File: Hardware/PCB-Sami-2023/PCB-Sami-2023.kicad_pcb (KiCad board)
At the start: 2 copper layers, 75.2 x 32 mm, 16 parts, among them J1 Bateria (+), J10 MOTOR_DER, J2 IR_COSTADO, J3 Sensor TATAMI FD, J5 Sensor TATAMI FI, J6 STEP_DOWN, J7 IR_FD, J8 IR_FI, J9 MOTOR_IZQ, SW1 START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

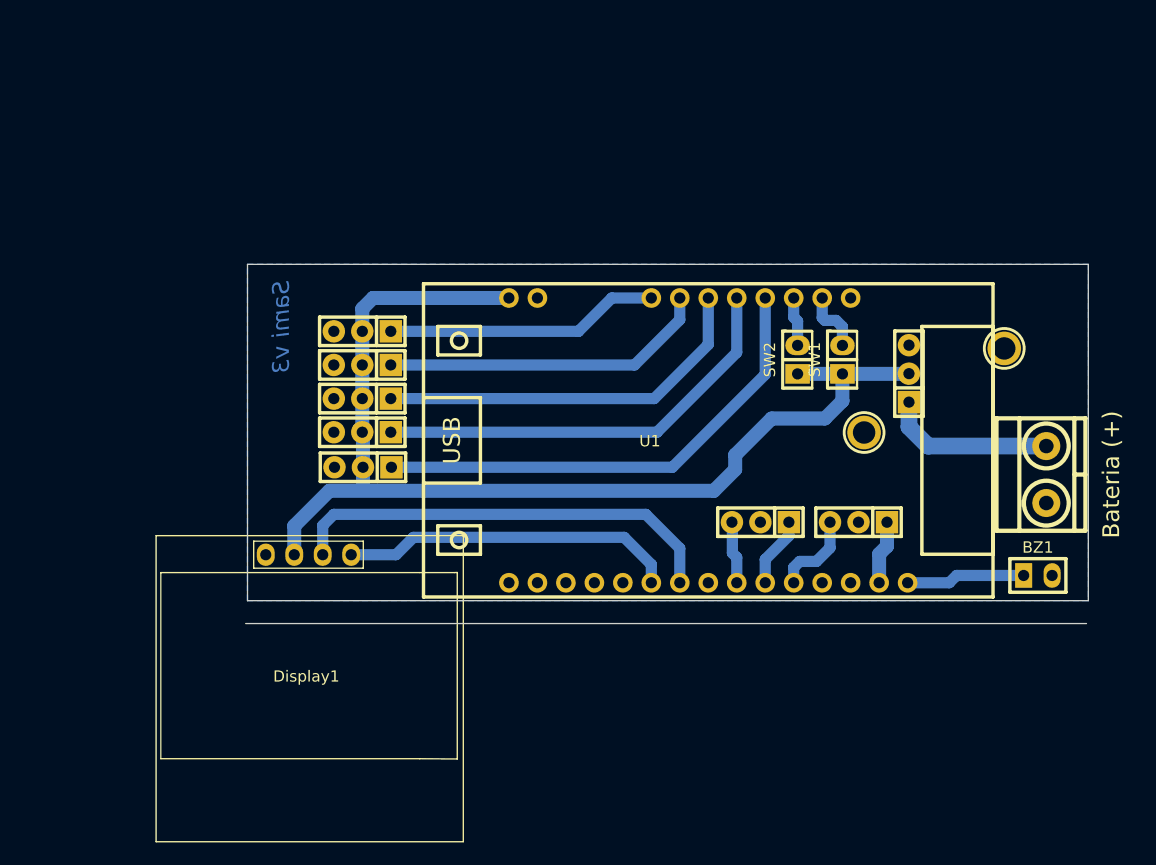
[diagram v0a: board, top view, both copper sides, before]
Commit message: PCB con sus componentes correctamente acomodados, falta solo los agujeros de sujecion y trazar pistas
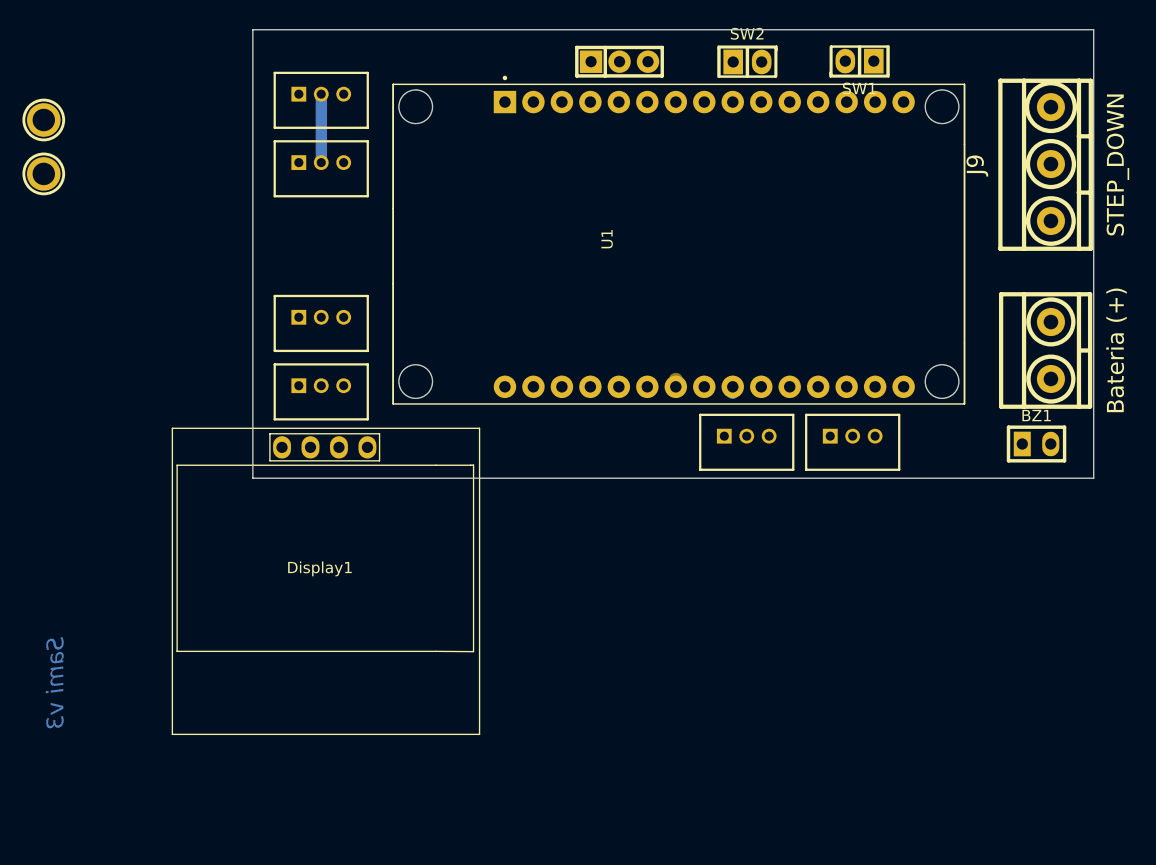
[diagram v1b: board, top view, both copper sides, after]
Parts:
- removed the J10 at (161.2, 95.8)
- removed J2: IR_COSTADO, EESTN5:Pin_Strip_3
- removed J3: Sensor TATAMI FD, EESTN5:Pin_Strip_3
- removed J5: Sensor TATAMI FI, EESTN5:Pin_Strip_3
- removed J6: STEP_DOWN, EESTN5:Pin_Strip_3
- removed J7: IR_FD, EESTN5:Pin_Strip_3
- removed J8: IR_FI, EESTN5:Pin_Strip_3
- added P1: SensorTatamiDerecho, Footprints:JstXH3P, F.Cu at (113.3, 77.5)
- added P2: SensorTatamiIzquierdo, Footprints:JstXH3P, F.Cu at (113.3, 83.6)
- added P3: IFR_DER, Footprints:JstXH3P, F.Cu at (113.3, 57.6)
- added P4: IFR_IZQ, Footprints:JstXH3P, F.Cu at (113.3, 63.7)
- added P5: LDR, EESTN5:Pin_Strip_3, F.Cu at (139.9, 54.7)
- added P6: MotorDerecho, Footprints:JstXH3P, F.Cu at (160.7, 88.1)
- added P7: MotorIzquierdo, Footprints:JstXH3P, F.Cu at (151.2, 88.1)
- J9: value MOTOR_IZQ -> STEP_DOWN; footprint EESTN5:Pin_Strip_3 -> EESTN5:BORNERA3_AZUL
- U1: value ESP32_DevKit_V1_CH9102X -> ESP32-DEVKIT-V1; footprint EESTN5:ESP32_DevKit_V1_CH9102X -> Footprints:ESP32-DEVKIT-V1-30Pines
- moved H1 88.1 mm to (88.5, 59.9)
- moved H2 76.7 mm to (88.5, 64.7)
- moved J9 41.1 mm to (178.4, 63.8), turned to 90 degrees
- moved SW2 27.2 mm to (151.3, 54.4), turned to 0 degrees
- moved SW1 26.4 mm to (161.3, 55.0), turned to 180 degrees
- moved U1 18.4 mm to (145.2, 70.5), turned to 90 degrees
- moved BZ1 11.7 mm to (177.1, 88.8)
- moved J10 11.1 mm to (178.4, 80.5)
- moved Display1 9.68 mm to (113.4, 99.7)
- renumbered J1 to J10
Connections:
- J9 pad 1: /M2B -> GND
- J9 pad 2: GND -> +5V
- J9 pad 3: /M2A -> /Vstep
- U1 pad 10: /TATAMI_FI -> /TATAMI_IZQ
- U1 pad 14: GND -> unconnected-(U1-VP-Pad14)
- U1 pad 15: +5V -> unconnected-(U1-EN-Pad15)
- U1 pad 16: unconnected-(U1-Pad16) -> /BUZZER
- U1 pad 17: GND -> /M1B_DIR
- U1 pad 20: unconnected-(U1-Pad20) -> /M1A_PWM
- U1 pad 21: /SDA -> /M2B_DIR
- U1 pad 22: /SCL -> /M2A_PWM
- U1 pad 24: /M2A -> /SCL
- U1 pad 25: /M2B -> /SDA
- U1 pad 26: /M1A -> unconnected-(U1-D4-Pad26)
- U1 pad 29: /M1B -> GND
- U1 pad 30: /BUZZER -> unconnected-(U1-3V3-Pad30)
- U1 pad 4: /START -> unconnected-(U1-D12-Pad4)
- U1 pad 5: /ESTRATEGIA -> unconnected-(U1-D14-Pad5)
- U1 pad 6: /IR_COSTADO -> /IR_IZQ
- U1 pad 7: /IR_FD -> /IR_DER
- U1 pad 8: /IR_FI -> /LDR
- U1 pad 9: /TATAMI_FD -> /TATAMI_DER
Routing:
- net +5V: track 99.7 -> 6.10 mm
- net /IR_COSTADO: track 43.6 -> 0.00 mm
- net /IR_FD: track 38.7 -> 0.00 mm
- net /SCL: track 39.2 -> 0.62 mm
- net /IR_FI: track 34.5 -> 0.00 mm
- net /SDA: track 30.0 -> 0.22 mm
- net /TATAMI_FD: track 29.4 -> 0.00 mm
- net /TATAMI_FI: track 24.5 -> 0.00 mm
- net /Vstep: track 15.2 -> 0.00 mm
- net /BUZZER: track 10.6 -> 0.00 mm
- net /M1A: track 7.62 -> 0.00 mm
- net /M2B: track 7.00 -> 0.00 mm
- net /M1B: track 5.69 -> 0.00 mm
- net /M2A: track 5.58 -> 0.00 mm
- net /START: track 5.56 -> 0.00 mm
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- removed copper zone on B.Cu, net GND
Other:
- board size 75.2 x 32 mm -> 75 x 40 mm

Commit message: placa terminada
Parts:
- removed BZ1: Buzzer, EESTN5:Pin_strip_2
- moved H1 73.7 mm to (161.9, 66.8)
- moved P5 43.8 mm to (169.2, 87.3), turned to 90 degrees
- moved H2 38.4 mm to (126.9, 66.8)
- moved SW2 27.6 mm to (177.9, 61.6), turned to 180 degrees
- moved SW1 16.8 mm to (177.9, 57.3)
- moved J9 8.02 mm to (177.5, 71.8)
- moved J10 5.31 mm to (177.5, 85.7)
- moved P4 2.60 mm to (113.2, 61.1)
- moved P2 2.60 mm to (113.2, 81.0)
- moved P3 2.60 mm to (113.2, 55.0)
- moved U1 2.57 mm to (144.9, 68.0)
- moved P1 2.50 mm to (113.2, 75.0)
- moved P7 1.38 mm to (150.9, 86.8)
- moved P6 1.38 mm to (160.4, 86.8)
- moved Display1 1.20 mm to (112.9, 98.6)
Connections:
- U1 pad 10: /TATAMI_IZQ -> /BUZZER
- U1 pad 16: /BUZZER -> /LDR
- U1 pad 6: /IR_IZQ -> /IR_DER
- U1 pad 7: /IR_DER -> /IR_IZQ
- U1 pad 8: /LDR -> /TATAMI_DER
- U1 pad 9: /TATAMI_DER -> /TATAMI_IZQ
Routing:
- net +5V: track 6.10 -> 142.5 mm
- net /TATAMI_IZQ: track 0.00 -> 51.4 mm
- net /TATAMI_DER: track 0.00 -> 45.8 mm
- net /SCL: track 0.62 -> 39.1 mm
- net /IR_IZQ: track 0.00 -> 33.1 mm
- net /IR_DER: track 0.00 -> 32.1 mm
- net /SDA: track 0.22 -> 32.0 mm
- net /ESTRATEGIA: track 0.00 -> 26.2 mm
- net GND: track 0.00 -> 25.4 mm
- net /START: track 0.00 -> 22.4 mm
- net /Vstep: track 0.00 -> 21.6 mm
- net /M1A_PWM: track 0.00 -> 8.30 mm
- net /LDR: track 0.00 -> 7.22 mm
- net /M2B_DIR: track 0.00 -> 5.91 mm
- net /M1B_DIR: track 0.00 -> 5.61 mm
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- added copper zone on B.Cu, net GND
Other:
- board text removed: "Sami v3"

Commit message: PCB terminado
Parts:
- removed Display1: SSD1306-SSD1306-128x64_OLED, EESTN5:128x64OLED
- added P8: Pantalla Oled, Footprints:JstXH4P, F.Cu at (113.2, 88.0)
- moved P6 1.20 mm to (159.2, 86.7)
- moved P7 1.20 mm to (149.8, 86.7)
- moved P5 0.50 mm to (168.7, 87.3)
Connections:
- P6 pad 1: /M1A_PWM -> GND
- P6 pad 2: GND -> /M1B_DIR
- P6 pad 3: /M1B_DIR -> /M1A_PWM
- P7 pad 1: /M2A_PWM -> GND
- P7 pad 2: GND -> /M2B_DIR
- P7 pad 3: /M2B_DIR -> /M2A_PWM
- U1 pad 10: /BUZZER -> unconnected-(U1-D32-Pad10)
- U1 pad 17: /M1B_DIR -> /M1A_PWM
- U1 pad 20: /M1A_PWM -> /M1B_DIR
- U1 pad 21: /M2B_DIR -> /M2A_PWM
- U1 pad 22: /M2A_PWM -> /M2B_DIR
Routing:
- net GND: track 25.4 -> 43.6 mm, vias 0 -> 4
- net +5V: track 142.5 -> 149.0 mm
- net /M1B_DIR: track 5.61 -> 8.62 mm
- net /M1A_PWM: track 8.30 -> 6.12 mm
- net /START: track 22.4 -> 24.2 mm
- net /SDA: track 32.0 -> 32.7 mm
- net /LDR: track 7.22 -> 6.57 mm

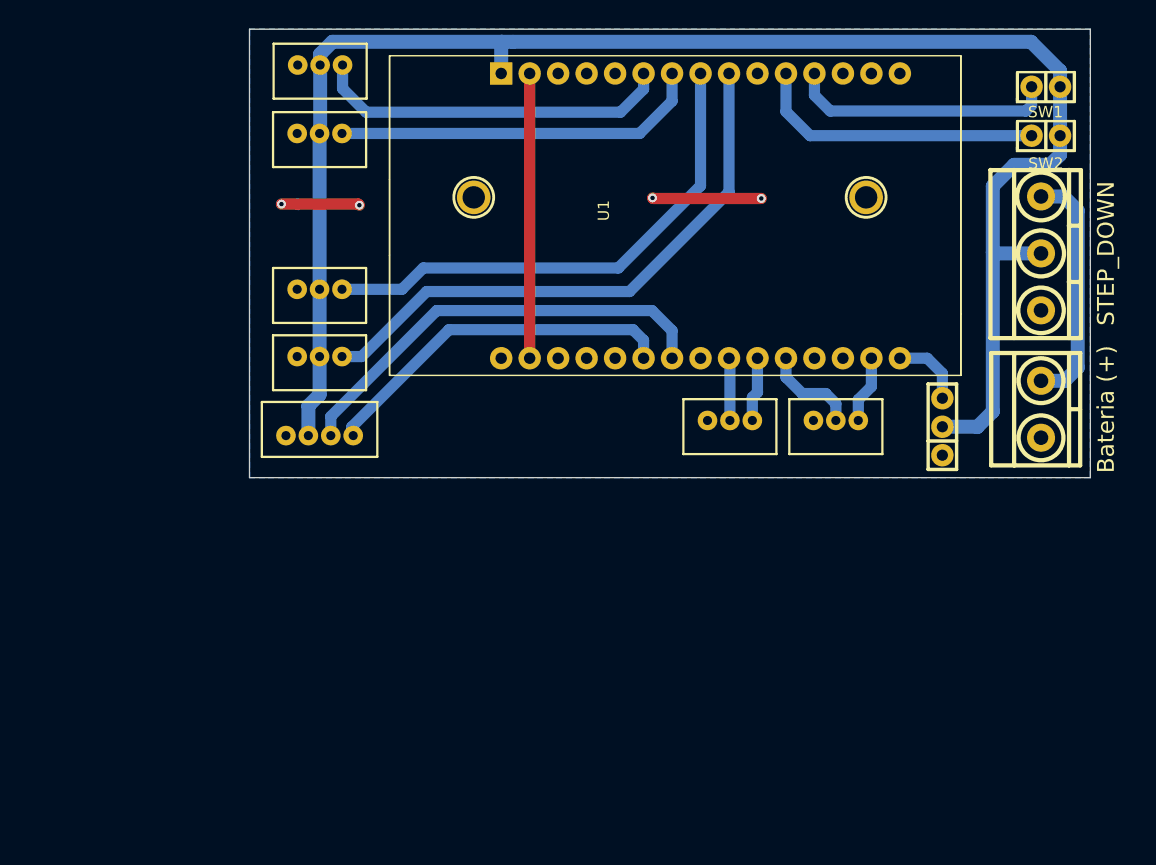
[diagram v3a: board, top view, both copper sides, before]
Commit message: Corregi algunos errores de la placa
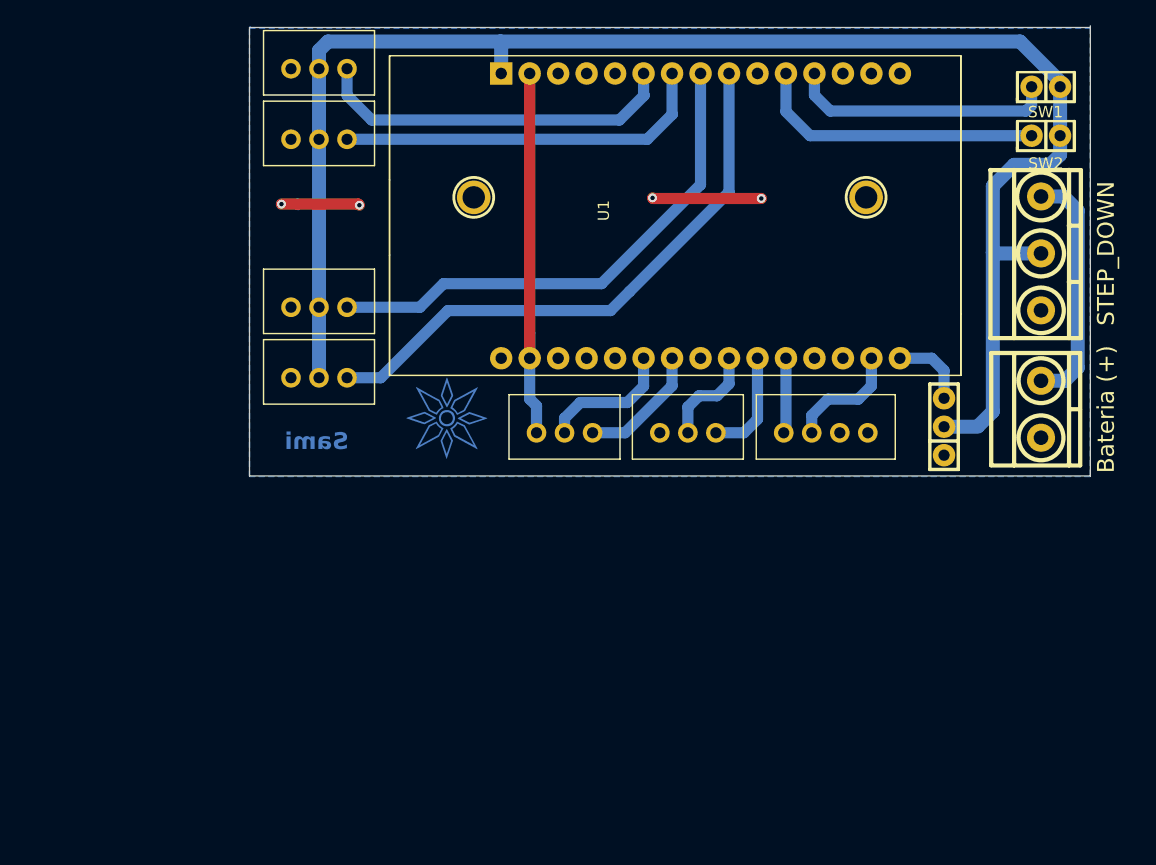
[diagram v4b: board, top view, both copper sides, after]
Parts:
- added G1: LOGO, footprints:LogoSami2, F.Cu at (124.5, 86.5)
- added REF**: Sami, footprints:Sami, F.Cu at (112.9, 88.5)
- P1, P2, P3, P4, P6, P7: footprint Footprints:JstXH3P -> footprints:JstXH3P
- P8: footprint Footprints:JstXH4P -> footprints:JstXH4P
- moved P8 45.2 mm to (158.3, 87.3), turned to 0 degrees
- moved P6 24.2 mm to (135.0, 87.3)
- moved P7 3.79 mm to (146.0, 87.3)
- moved P2 1.37 mm to (113.1, 82.4)
- moved P1 1.08 mm to (113.1, 76.1)
- moved P3 0.22 mm to (113.1, 54.8)
- moved P5 0.15 mm to (168.8, 87.3)
- moved P4 0.05 mm to (113.1, 61.1)
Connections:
- net /M2A_PWM renamed /M2B_PWM
- net /M2B_DIR renamed /M2A_DIR
- P6 pad 2: /M1B_DIR -> /M1A_DIR
- P6 pad 3: /M1A_PWM -> /M1B_PWM
- U1 pad 17: /M1A_PWM -> /SCL
- U1 pad 20: /M1B_DIR -> /SDA
- U1 pad 24: /SCL -> /M1B_PWM
- U1 pad 25: /SDA -> /M1A_DIR
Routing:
- net /SCL: track 39.3 -> 10.5 mm
- net /SDA: track 32.7 -> 6.73 mm
- net /M1A_DIR: track 0.00 -> 12.0 mm
- net /M1B_PWM: track 0.00 -> 11.3 mm
- net GND: track 43.6 -> 54.1 mm
- net /M1B_DIR: track 8.62 -> 0.00 mm
- net /M1A_PWM: track 6.12 -> 0.00 mm
- net +5V: track 149.0 -> 143.0 mm
- net /M2B_PWM: track 5.80 -> 9.71 mm
- net /M2A_DIR: track 5.58 -> 9.32 mm
- net /IR_DER: track 32.1 -> 32.7 mm
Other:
- board size 75 x 40 mm -> 75 x 40.2 mm

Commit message: agregue el svg para la fabricacion del pcb
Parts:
- P1: value SensorTatamiDerecho -> TatamiDerecho
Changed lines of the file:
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@@
         (effects (font (size 1 1) (thickness 0.15)))
     )
-    (fp_text value "SensorTatamiDerecho" (at 0 3.78) (layer "F.Fab")
+    (fp_text value "TatamiDerecho" (at 0 -4.275) (layer "F.Fab")
         (effects (font (size 1 1) (thickness 0.15)))
     )
@@
     (pts (xy 126.9 66.8) (xy 106.9 66.8))
     (height 20.049998)
-    (gr_text "20.0000 mm" (at 116.9 45.600002) (layer "Edge.Cuts")
+    (gr_text "20,0000 mm" (at 116.9 45.600002) (layer "Edge.Cuts")
       (effects (font (size 1 1) (thickness 0.15)))
     )
@@
     (pts (xy 106.9 51.8) (xy 181.9 51.8))
     (height -9.95)
-    (gr_text "75.0000 mm" (at 144.4 40.7) (layer "Edge.Cuts")
+    (gr_text "75,0000 mm" (at 144.4 40.7) (layer "Edge.Cuts")
       (effects (font (size 1 1) (thickness 0.15)))
     )
@@
     (pts (xy 156.85 66.65) (xy 156.85 51.65))
     (height 25.05)
-    (gr_text "15.0000 mm" (at 180.75 59.15 90) (layer "Edge.Cuts")
+    (gr_text "15,0000 mm" (at 180.75 59.15 90) (layer "Edge.Cuts")
       (effects (font (size 1 1) (thickness 0.15)))
     )
@@
     (pts (xy 161.9 66.8) (xy 181.9 66.8))
     (height -20.05)
-    (gr_text "20.0000 mm" (at 171.9 45.6) (layer "Edge.Cuts")
+    (gr_text "20,0000 mm" (at 171.9 45.6) (layer "Edge.Cuts")
       (effects (font (size 1 1) (thickness 0.15)))
     )
@@
     (pts (xy 181.9 91.65) (xy 181.9 51.65))
     (height 10)
-    (gr_text "40.0000 mm" (at 190.75 71.65 90) (layer "Edge.Cuts")
+    (gr_text "40,0000 mm" (at 190.75 71.65 90) (layer "Edge.Cuts")
       (effects (font (size 1 1) (thickness 0.15)))
     )
@@
     (pts (xy 161.9 66.8) (xy 126.9 66.8))
     (height 20.049999)
-    (gr_text "35.0000 mm" (at 144.4 45.600001) (layer "Edge.Cuts")
+    (gr_text "35,0000 mm" (at 144.4 45.600001) (layer "Edge.Cuts")
       (effects (font (size 1 1) (thickness 0.15)))
     )

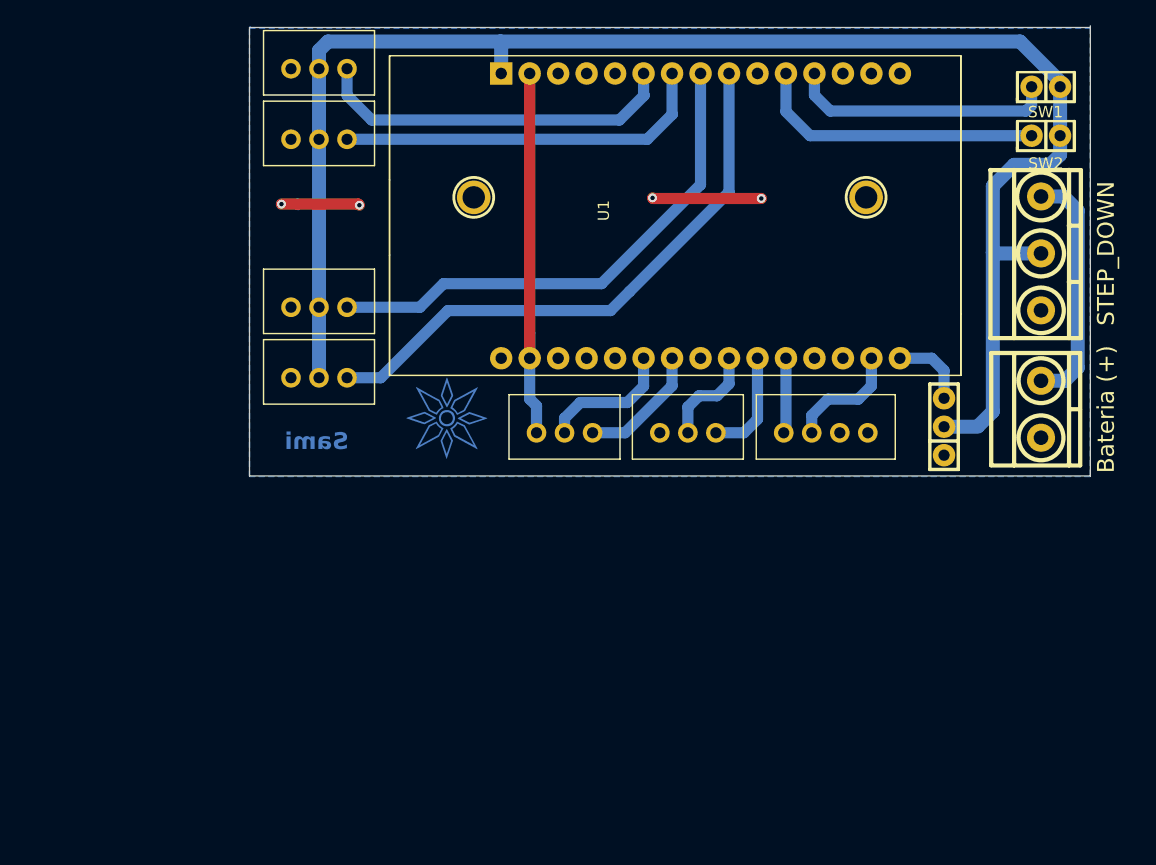
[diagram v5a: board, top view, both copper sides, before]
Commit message: agregue el archivo svg para la seligrafia
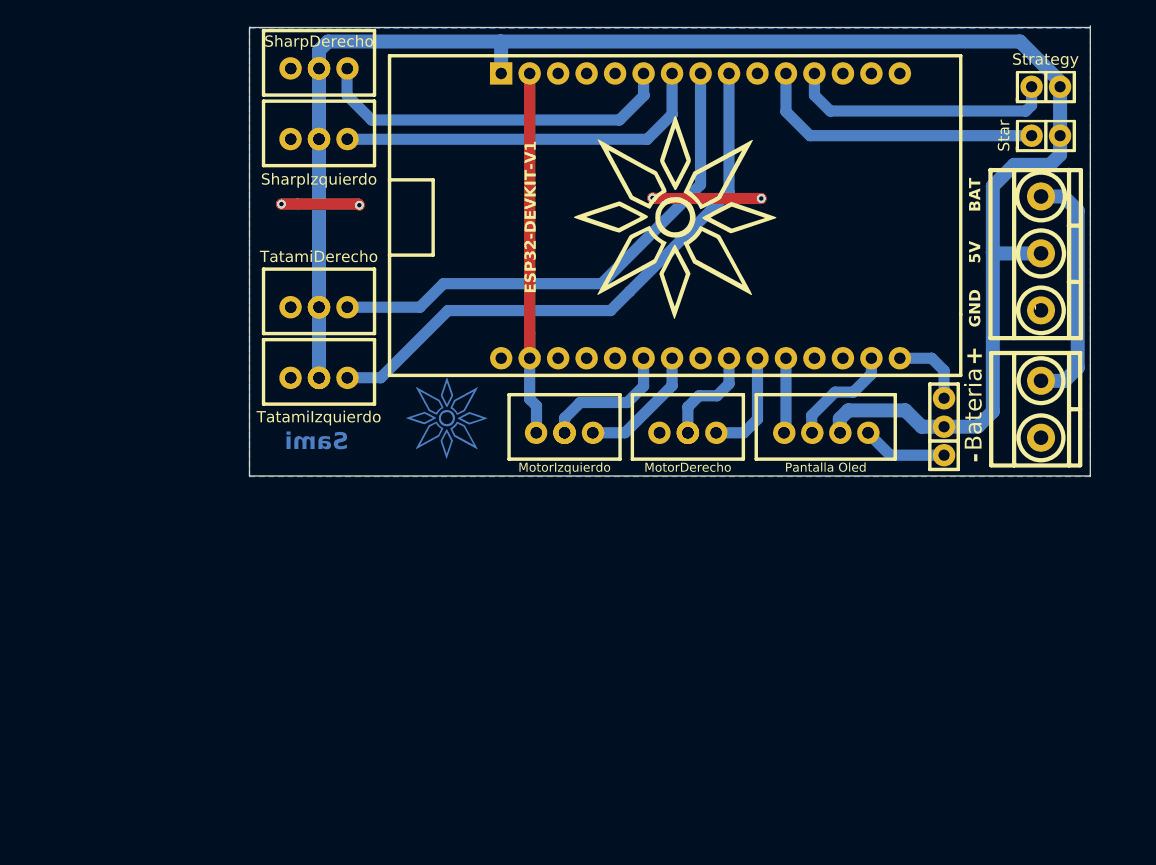
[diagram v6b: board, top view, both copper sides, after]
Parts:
- removed H1, H2: Mounting_Hole, EESTN5:pad_3mm
- added ?: , , F.Cu at (110.6, 76.6)
- added ?: , , F.Cu at (148.5, 87.8)
- added ?: , , F.Cu at (162.1, 87.8)
- added ?: , , F.Cu at (132.5, 87.8)
- added ? (x2): , , F.Cu at (113.1, 55.3)
- added ?: , , F.Cu at (115.6, 82.9)
- added ? (x2): , , F.Cu at (113.1, 61.6)
- added ?: , , F.Cu at (115.6, 76.6)
- added ?: , , F.Cu at (157.1, 87.8)
- added ?: , , F.Cu at (110.6, 82.9)
- added ?: , , F.Cu at (143.5, 87.8)
- added ? (x2): , , F.Cu at (113.1, 76.6)
- added ? (x2): , , F.Cu at (113.1, 82.9)
- added ? (x2): , , F.Cu at (146.0, 87.8)
- added ?: , , F.Cu at (115.6, 55.3)
- added ? (x2): , , F.Cu at (135.0, 87.8)
- added ?: , , F.Cu at (137.5, 87.8)
- added ?: , , F.Cu at (110.6, 61.6)
- added ?: , , F.Cu at (159.6, 87.8)
- added ?: , , F.Cu at (154.6, 87.8)
- added ?: , , F.Cu at (115.6, 61.6)
- added ?: , , F.Cu at (110.6, 55.3)
- added G***: LOGO, footprints:SamiSeligrafia, F.Cu at (144.9, 68.6)
- J10: value Bateria (+) -> Bateria
- P2: value SensorTatamiIzquierdo -> TatamiIzquierdo
- P3: value IFR_DER -> SharpDerecho
- P4: value IFR_IZQ -> SharpIzquierdo
- P6: value MotorDerecho -> MotorIzquierdo
- P7: value MotorIzquierdo -> MotorDerecho
- renumbered SW2 to Star, SW1 to Strategy
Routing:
- net +5V: track 143.0 -> 154.5 mm
- net GND: track 54.1 -> 61.7 mm
- net /SCL: track 10.5 -> 9.85 mm
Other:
- board text added: "+"
- board text added: "-"
- board text added: "5V"
- board text added: "BAT"
- board text added: "GND"
